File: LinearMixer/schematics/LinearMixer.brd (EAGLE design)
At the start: 49.7 x 98.7 mm, 65 parts, among them IC1 QUAD_OPAMPD, IC2 QUAD_OPAMPD, X1 53048-05, X2 53048-05, X5 53048-03, X6 53048-03, X7 53048-03

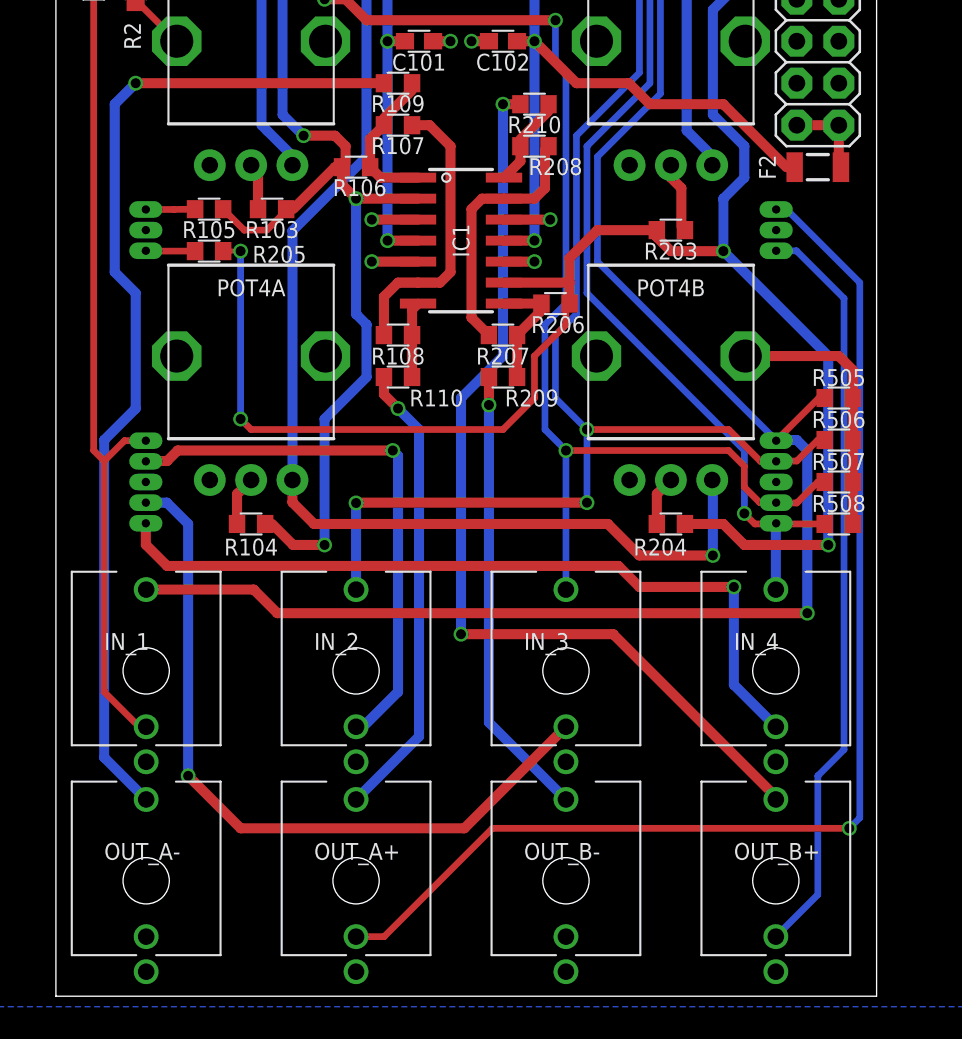
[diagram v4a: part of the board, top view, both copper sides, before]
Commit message: adjusted routing and labels, moved connector away from power inlet
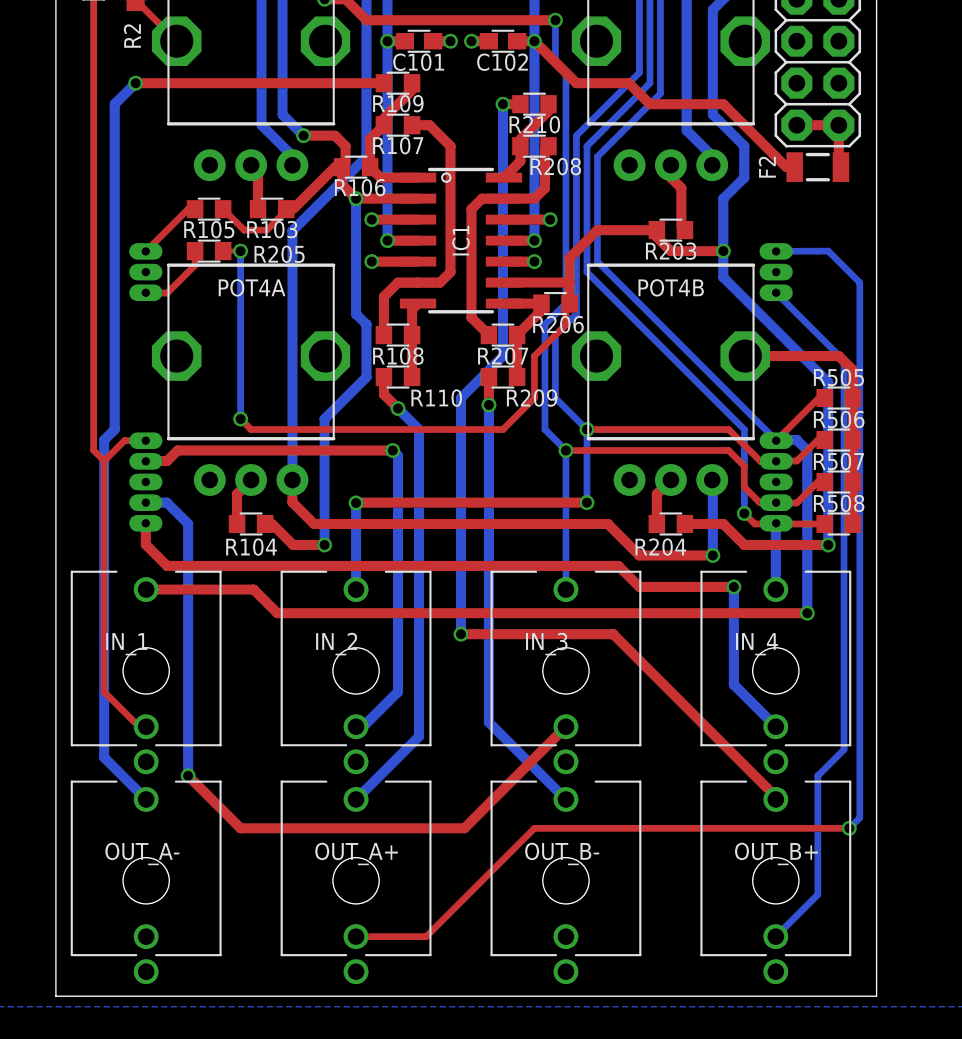
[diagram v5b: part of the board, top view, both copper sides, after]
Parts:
- moved X6 2.54 mm to (6.35, 44.5)
- moved X7 2.54 mm to (47.0, 44.5)
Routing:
- net OUT_SW_B: track 45.6 -> 42.4 mm
- net IN_B: track 2.99 -> 4.54 mm
- net OUT_SW_A: track 72.8 -> 71.7 mm
- net IN_A: track 2.98 -> 4.04 mm
- net N$11: track 61.3 -> 60.2 mm
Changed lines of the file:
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@@
 <layer number="27" name="tValues" color="7" fill="1" visible="no" active="yes"/>
 <layer number="28" name="bValues" color="7" fill="1" visible="no" active="yes"/>
-<layer number="29" name="tStop" color="7" fill="3" visible="yes" active="yes"/>
-<layer number="30" name="bStop" color="7" fill="6" visible="yes" active="yes"/>
+<layer number="29" name="tStop" color="7" fill="3" visible="no" active="yes"/>
+<layer number="30" name="bStop" color="7" fill="6" visible="no" active="yes"/>
 <layer number="31" name="tCream" color="7" fill="4" visible="no" active="yes"/>
 <layer number="32" name="bCream" color="7" fill="5" visible="no" active="yes"/>
@@
 <wire x1="2.159" y1="0.635" x2="51.816" y2="0.635" width="0" layer="20"/>
 <dimension x1="1.27" y1="0" x2="1.27" y2="100" x3="-1.27" y3="50" textsize="1.778" layer="47"/>
-<dimension x1="2.032" y1="0" x2="51.816" y2="0" x3="26.924" y3="-4.445" textsize="1.778" layer="47"/>
+<dimension x1="1.816" y1="0" x2="51.816" y2="0" x3="26.816" y3="-4.445" textsize="1.778" layer="47"/>
 <text x="4.445" y="70.485" size="1.778" layer="47" font="vector" rot="R90">Rebel Technology</text>
 <text x="6.985" y="70.485" size="1.778" layer="47" font="vector" rot="R90">LinearMixer Rev02</text>
@@
 <attribute name="NAME" x="49.53" y="37.563425" size="1.016" layer="25" font="vector" align="bottom-center"/>
 </element>
-<element name="X6" library="con-molex" package="53048-03" value="53048-03" x="6.35" y="46.99" rot="MR270">
-<attribute name="OC_NEWARK" value="38C9908" x="6.35" y="46.99" size="1.016" layer="28" rot="MR270" display="off"/>
-<attribute name="MPN" value="53048-0310" x="6.35" y="46.99" size="1.016" layer="28" rot="MR270" display="off"/>
-<attribute name="MF" value="WALDOM/MOLEX" x="6.35" y="46.99" size="1.016" layer="28" rot="MR270" display="off"/>
-<attribute name="OC_FARNELL" value="9732918" x="6.35" y="46.99" size="1.016" layer="28" rot="MR270" display="off"/>
-</element>
-<element name="X7" library="con-molex" package="53048-03" value="53048-03" x="46.99" y="46.99" rot="MR90">
-<attribute name="OC_NEWARK" value="38C9908" x="46.99" y="46.99" size="1.016" layer="28" rot="MR90" display="off"/>
-<attribute name="MPN" value="53048-0310" x="46.99" y="46.99" size="1.016" layer="28" rot="MR90" display="off"/>
-<attribute name="MF" value="WALDOM/MOLEX" x="46.99" y="46.99" size="1.016" layer="28" rot="MR90" display="off"/>
-<attribute name="OC_FARNELL" value="9732918" x="46.99" y="46.99" size="1.016" layer="28" rot="MR90" display="off"/>
+<element name="X6" library="con-molex" package="53048-03" value="53048-03" x="6.35" y="44.45" rot="MR270">
+<attribute name="OC_NEWARK" value="38C9908" x="6.35" y="44.45" size="1.016" layer="28" rot="MR270" display="off"/>
+<attribute name="MPN" value="53048-0310" x="6.35" y="44.45" size="1.016" layer="28" rot="MR270" display="off"/>
+<attribute name="MF" value="WALDOM/MOLEX" x="6.35" y="44.45" size="1.016" layer="28" rot="MR270" display="off"/>
+<attribute name="OC_FARNELL" value="9732918" x="6.35" y="44.45" size="1.016" layer="28" rot="MR270" display="off"/>
+</element>
+<element name="X7" library="con-molex" package="53048-03" value="53048-03" x="46.99" y="44.45" rot="MR90">
+<attribute name="OC_NEWARK" value="38C9908" x="46.99" y="44.45" size="1.016" layer="28" rot="MR90" display="off"/>
+<attribute name="MPN" value="53048-0310" x="46.99" y="44.45" size="1.016" layer="28" rot="MR90" display="off"/>
+<attribute name="MF" value="WALDOM/MOLEX" x="46.99" y="44.45" size="1.016" layer="28" rot="MR90" display="off"/>
+<attribute name="OC_FARNELL" value="9732918" x="46.99" y="44.45" size="1.016" layer="28" rot="MR90" display="off"/>
 </element>
 </elements>
@@
 <via x="6.985" y="55.88" extent="1-16" drill="0.6"/>
 <wire x1="6.985" y1="55.88" x2="5.715" y2="54.61" width="0.6096" layer="16"/>
-<wire x1="5.715" y1="54.61" x2="5.715" y2="44.45" width="0.6096" layer="16"/>
-<wire x1="5.715" y1="44.45" x2="6.985" y2="43.18" width="0.6096" layer="16"/>
-<wire x1="6.985" y1="43.18" x2="6.985" y2="36.195" width="0.6096" layer="16"/>
-<wire x1="6.985" y1="36.195" x2="5.08" y2="34.29" width="0.6096" layer="16"/>
+<wire x1="5.715" y1="54.61" x2="5.715" y2="34.925" width="0.6096" layer="16"/>
+<wire x1="5.715" y1="34.925" x2="5.08" y2="34.29" width="0.6096" layer="16"/>
 <wire x1="5.08" y1="34.29" x2="5.08" y2="15.08" width="0.6096" layer="16"/>
 <wire x1="5.08" y1="15.08" x2="7.62" y2="12.54" width="0.6096" layer="16"/>
@@
 <wire x1="38.1" y1="64.77" x2="38.1" y2="55.88" width="0.4064" layer="16"/>
 <wire x1="38.1" y1="55.88" x2="34.29" y2="52.07" width="0.4064" layer="16"/>
-<wire x1="34.29" y1="52.07" x2="34.29" y2="43.18" width="0.4064" layer="16"/>
-<wire x1="34.29" y1="43.18" x2="43.815" y2="33.655" width="0.4064" layer="16"/>
+<wire x1="34.29" y1="52.07" x2="34.29" y2="44.45" width="0.4064" layer="16"/>
+<wire x1="34.29" y1="44.45" x2="43.815" y2="34.925" width="0.4064" layer="16"/>
 <contactref element="R508" pad="1"/>
-<wire x1="43.815" y1="33.655" x2="43.815" y2="29.845" width="0.4064" layer="16"/>
+<wire x1="43.815" y1="34.925" x2="43.815" y2="29.845" width="0.4064" layer="16"/>
 <wire x1="43.815" y1="29.845" x2="44.45" y2="29.21" width="0.4064" layer="1"/>
 <wire x1="44.45" y1="29.21" x2="45.7" y2="29.21" width="0.4064" layer="1"/>
@@
 <wire x1="43.815" y1="27.94" x2="48.895" y2="27.94" width="0.6096" layer="1"/>
 <via x="48.895" y="27.94" extent="1-16" drill="0.6"/>
-<wire x1="48.895" y1="27.94" x2="48.895" y2="39.37" width="0.6096" layer="16"/>
-<wire x1="48.895" y1="39.37" x2="42.545" y2="45.72" width="0.6096" layer="16"/>
+<wire x1="48.895" y1="27.94" x2="48.895" y2="37.7825" width="0.6096" layer="16"/>
+<wire x1="48.895" y1="37.7825" x2="42.545" y2="44.1325" width="0.6096" layer="16"/>
+<wire x1="42.545" y1="44.1325" x2="42.545" y2="45.72" width="0.6096" layer="16"/>
 <wire x1="12.28" y1="45.72" x2="13.335" y2="45.72" width="0.3048" layer="1"/>
 <via x="13.335" y="45.72" extent="1-16" drill="0.6"/>
@@
 <signal name="IN_A">
 <contactref element="R105" pad="2"/>
-<wire x1="9.29" y1="48.24" x2="10.58" y2="48.26" width="0.4064" layer="1"/>
 <contactref element="X6" pad="3"/>
-<wire x1="9.29" y1="48.24" x2="7.6" y2="48.24" width="0.4064" layer="1"/>
+<wire x1="10.58" y1="48.26" x2="10.16" y2="48.26" width="0.4064" layer="1"/>
+<wire x1="10.16" y1="48.26" x2="7.6" y2="45.7" width="0.4064" layer="1"/>
 </signal>
 <signal name="IN_B">
 <contactref element="R205" pad="2"/>
-<wire x1="10.58" y1="45.72" x2="7.62" y2="45.72" width="0.4064" layer="1"/>
 <contactref element="X6" pad="1"/>
-<wire x1="7.62" y1="45.72" x2="7.6" y2="45.74" width="0.4064" layer="1"/>
+<wire x1="10.58" y1="45.72" x2="10.58" y2="44.87" width="0.4064" layer="1"/>
+<wire x1="10.58" y1="44.87" x2="8.89" y2="43.18" width="0.4064" layer="1"/>
+<wire x1="8.89" y1="43.18" x2="7.62" y2="43.18" width="0.4064" layer="1"/>
+<wire x1="7.62" y1="43.18" x2="7.6" y2="43.2" width="0.4064" layer="1"/>
 </signal>
 <signal name="OUT_SW_A">
@@
 <wire x1="50.8" y1="43.815" x2="50.8" y2="11.43" width="0.4064" layer="16"/>
 <wire x1="50.8" y1="11.43" x2="50.165" y2="10.795" width="0.4064" layer="16"/>
-<wire x1="46.355" y1="48.26" x2="50.8" y2="43.815" width="0.4064" layer="16"/>
-<wire x1="20.32" y1="4.24" x2="22.02" y2="4.24" width="0.4064" layer="1"/>
-<wire x1="22.02" y1="4.24" x2="28.575" y2="10.795" width="0.4064" layer="1"/>
-<wire x1="28.575" y1="10.795" x2="50.165" y2="10.795" width="0.4064" layer="1"/>
+<wire x1="48.895" y1="45.72" x2="50.8" y2="43.815" width="0.4064" layer="16"/>
+<wire x1="20.32" y1="4.24" x2="24.56" y2="4.24" width="0.4064" layer="1"/>
+<wire x1="24.56" y1="4.24" x2="31.115" y2="10.795" width="0.4064" layer="1"/>
+<wire x1="31.115" y1="10.795" x2="50.165" y2="10.795" width="0.4064" layer="1"/>
 <via x="50.165" y="10.795" extent="1-16" drill="0.6"/>
 <contactref element="X7" pad="1"/>
-<wire x1="45.74" y1="48.24" x2="45.72" y2="48.26" width="0.4064" layer="16"/>
-<wire x1="45.72" y1="48.26" x2="46.355" y2="48.26" width="0.4064" layer="16"/>
+<wire x1="45.74" y1="45.7" x2="48.26" y2="45.72" width="0.4064" layer="16"/>
+<wire x1="48.26" y1="45.72" x2="48.895" y2="45.72" width="0.4064" layer="16"/>
 </signal>
 <signal name="OUT_SW_B">
 <contactref element="OUT_B+" pad="P$2"/>
-<wire x1="49.8475" y1="15.5575" x2="49.8475" y2="42.8625" width="0.4064" layer="16"/>
+<wire x1="49.8475" y1="15.5575" x2="49.8475" y2="39.0925" width="0.4064" layer="16"/>
 <wire x1="49.8475" y1="15.5575" x2="48.26" y2="13.97" width="0.4064" layer="16"/>
 <wire x1="48.26" y1="13.97" x2="48.26" y2="6.78" width="0.4064" layer="16"/>
 <wire x1="48.26" y1="6.78" x2="45.72" y2="4.24" width="0.4064" layer="16"/>
 <contactref element="X7" pad="3"/>
-<wire x1="45.74" y1="45.74" x2="46.97" y2="45.74" width="0.4064" layer="16"/>
-<wire x1="46.97" y1="45.74" x2="49.8475" y2="42.8625" width="0.4064" layer="16"/>
+<wire x1="49.8475" y1="39.0925" x2="45.74" y2="43.2" width="0.4064" layer="16"/>
 </signal>
 <signal name="N$7">

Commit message: rev02 ordered from seeed
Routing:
- net IN_2: track 75.2 -> 72.7 mm, vias 4 -> 3
- net IN_4: vias 2 -> 1
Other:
- board text added: "-12V"
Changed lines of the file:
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@@
 <dimension x1="1.27" y1="0" x2="1.27" y2="100" x3="-1.27" y3="50" textsize="1.778" layer="47"/>
 <dimension x1="1.816" y1="0" x2="51.816" y2="0" x3="26.816" y3="-4.445" textsize="1.778" layer="47"/>
-<text x="4.445" y="70.485" size="1.778" layer="47" font="vector" rot="R90">Rebel Technology</text>
-<text x="6.985" y="70.485" size="1.778" layer="47" font="vector" rot="R90">LinearMixer Rev02</text>
-<text x="13.97" y="85.725" size="1.778" layer="47" font="vector" rot="MR180">Rebel Technology</text>
-<text x="12.7" y="82.55" size="1.778" layer="47" font="vector" rot="MR180">LinearMixer Rev02</text>
+<text x="4.445" y="70.485" size="1.778" layer="21" font="vector" rot="R90">Rebel Technology</text>
+<text x="6.985" y="70.485" size="1.778" layer="21" font="vector" rot="R90">LinearMixer Rev02</text>
+<text x="13.97" y="85.725" size="1.778" layer="22" font="vector" rot="MR180">Rebel Technology</text>
+<text x="12.7" y="82.55" size="1.778" layer="22" font="vector" rot="MR180">LinearMixer Rev02</text>
+<text x="48.26" y="49.276" size="1.27" layer="25" font="vector" align="top-center">-12V</text>
+<text x="48.26" y="49.276" size="1.27" layer="22" font="vector" rot="MR0" align="top-center">-12V</text>
 </plain>
 <attributes>
@@
 </element>
 <element name="IN_2" library="Rebel" package="THONKICONN" value="THONKICONN" x="20.32" y="20.32" smashed="yes">
-<attribute name="NAME" x="17.78" y="21.59" size="1.016" layer="25"/>
+<attribute name="NAME" x="17.78" y="22.86" size="1.016" layer="25"/>
 </element>
 <element name="IN_3" library="Rebel" package="THONKICONN" value="THONKICONN" x="33.02" y="20.32" smashed="yes">
-<attribute name="NAME" x="30.48" y="21.59" size="1.016" layer="25"/>
+<attribute name="NAME" x="30.48" y="22.86" size="1.016" layer="25"/>
 </element>
 <element name="IN_4" library="Rebel" package="THONKICONN" value="THONKICONN" x="45.72" y="20.32" smashed="yes">
-<attribute name="NAME" x="43.18" y="21.59" size="1.016" layer="25"/>
+<attribute name="NAME" x="43.18" y="22.86" size="1.016" layer="25"/>
 </element>
 <element name="IN_1" library="Rebel" package="THONKICONN" value="THONKICONN" x="7.62" y="20.32" smashed="yes">
-<attribute name="NAME" x="5.08" y="21.59" size="1.016" layer="25"/>
+<attribute name="NAME" x="5.08" y="22.86" size="1.016" layer="25"/>
 </element>
 <element name="IC2" library="adafruit" package="SO14" value="QUAD_OPAMPD" x="26.67" y="67.31" smashed="yes" rot="R270">
@@
 </element>
 <element name="OUT_A+" library="Rebel" package="THONKICONN" value="THONKICONN" x="20.32" y="7.62" smashed="yes">
-<attribute name="NAME" x="17.78" y="8.89" size="1.016" layer="25"/>
+<attribute name="NAME" x="17.78" y="10.16" size="1.016" layer="25"/>
 </element>
 <element name="OUT_A-" library="Rebel" package="THONKICONN" value="THONKICONN" x="7.62" y="7.62" smashed="yes">
-<attribute name="NAME" x="5.08" y="8.89" size="1.016" layer="25"/>
+<attribute name="NAME" x="5.08" y="10.16" size="1.016" layer="25"/>
 </element>
 <element name="OUT_B+" library="Rebel" package="THONKICONN" value="THONKICONN" x="45.72" y="7.62" smashed="yes">
-<attribute name="NAME" x="43.18" y="8.89" size="1.016" layer="25"/>
+<attribute name="NAME" x="43.18" y="10.16" size="1.016" layer="25"/>
 </element>
 <element name="OUT_B-" library="Rebel" package="THONKICONN" value="THONKICONN" x="33.02" y="7.62" smashed="yes">
-<attribute name="NAME" x="30.48" y="8.89" size="1.016" layer="25"/>
+<attribute name="NAME" x="30.48" y="10.16" size="1.016" layer="25"/>
 </element>
 <element name="R104" library="resistor" package="R0603" value="100k" x="13.97" y="29.21" smashed="yes" rot="R180">
@@
 <contactref element="R505" pad="1"/>
 <wire x1="45.74" y1="34.25" x2="45.74" y2="34.27" width="0.4064" layer="16"/>
-<wire x1="47.625" y1="23.8125" x2="47.625" y2="33.655" width="0.6096" layer="16"/>
-<wire x1="47.625" y1="33.655" x2="46.99" y2="34.29" width="0.6096" layer="16"/>
-<wire x1="46.99" y1="34.29" x2="45.78" y2="34.29" width="0.6096" layer="16"/>
+<wire x1="47.625" y1="23.8125" x2="47.625" y2="33.655" width="0.4064" layer="16"/>
+<wire x1="47.625" y1="33.655" x2="46.99" y2="34.29" width="0.4064" layer="16"/>
+<wire x1="46.99" y1="34.29" x2="45.78" y2="34.29" width="0.4064" layer="16"/>
 <wire x1="45.78" y1="34.29" x2="45.74" y2="34.25" width="0.6096" layer="16"/>
 <wire x1="48.68" y1="36.83" x2="48.32" y2="36.83" width="0.4064" layer="1"/>
@@
 <contactref element="R508" pad="1"/>
 <wire x1="43.815" y1="34.925" x2="43.815" y2="29.845" width="0.4064" layer="16"/>
-<wire x1="43.815" y1="29.845" x2="44.45" y2="29.21" width="0.4064" layer="1"/>
-<wire x1="44.45" y1="29.21" x2="45.7" y2="29.21" width="0.4064" layer="1"/>
+<wire x1="43.815" y1="29.845" x2="44.45" y2="29.21" width="0.4064" layer="16"/>
+<wire x1="44.45" y1="29.21" x2="45.7" y2="29.21" width="0.4064" layer="16"/>
+<wire x1="45.7" y1="29.21" x2="45.74" y2="29.25" width="0.4064" layer="16"/>
+<wire x1="48.68" y1="29.21" x2="45.78" y2="29.21" width="0.4064" layer="1"/>
+<wire x1="45.78" y1="29.21" x2="45.74" y2="29.25" width="0.4064" layer="1"/>
 <wire x1="45.72" y1="25.24" x2="45.72" y2="29.23" width="0.6096" layer="16"/>
 <wire x1="45.72" y1="29.23" x2="45.74" y2="29.25" width="0.6096" layer="16"/>
-<wire x1="48.68" y1="29.21" x2="45.78" y2="29.21" width="0.4064" layer="1"/>
-<via x="43.815" y="29.845" extent="1-16" drill="0.6"/>
-<wire x1="45.7" y1="29.21" x2="45.74" y2="29.25" width="0.6096" layer="1"/>
-<wire x1="45.74" y1="29.25" x2="45.78" y2="29.21" width="0.6096" layer="1"/>
 </signal>
 <signal name="IN_3">
@@
 <contactref element="R503" pad="2"/>
 <contactref element="X2" pad="4"/>
-<wire x1="33.02" y1="33.655" x2="33.02" y2="25.24" width="0.4064" layer="16"/>
+<wire x1="33.02" y1="33.655" x2="33.02" y2="25.24" width="0.6096" layer="16"/>
 <wire x1="19.47" y1="65.405" x2="18.415" y2="65.405" width="0.6096" layer="1"/>
 <via x="18.415" y="65.405" extent="1-16" drill="0.6"/>
@@
 <contactref element="R502" pad="2"/>
 <contactref element="X2" pad="2"/>
-<wire x1="34.29" y1="30.5" x2="20.34" y2="30.5" width="0.6096" layer="1"/>
 <wire x1="20.34" y1="30.5" x2="20.32" y2="30.48" width="0.3048" layer="1"/>
 <via x="20.32" y="30.48" extent="1-16" drill="0.6"/>
@@
 <wire x1="32.385" y1="40.64" x2="32.385" y2="36.83" width="0.4064" layer="16"/>
 <wire x1="32.385" y1="36.83" x2="34.29" y2="34.925" width="0.4064" layer="16"/>
-<via x="34.29" y="30.5" extent="1-16" drill="0.6"/>
 <contactref element="R506" pad="1"/>
-<wire x1="34.29" y1="34.925" x2="34.29" y2="30.5" width="0.4064" layer="16"/>
 <wire x1="45.74" y1="33" x2="44.7875" y2="33" width="0.4064" layer="1"/>
 <wire x1="44.7875" y1="33" x2="42.8625" y2="34.925" width="0.4064" layer="1"/>
@@
 <wire x1="46.99" y1="33.02" x2="45.76" y2="33.02" width="0.4064" layer="1"/>
 <wire x1="45.76" y1="33.02" x2="45.74" y2="33" width="0.4064" layer="1"/>
+<wire x1="34.29" y1="34.925" x2="32.385" y2="34.925" width="0.6096" layer="1"/>
+<wire x1="32.385" y1="34.925" x2="27.94" y2="30.48" width="0.6096" layer="1"/>
+<wire x1="27.94" y1="30.48" x2="20.32" y2="30.48" width="0.6096" layer="1"/>
 </signal>
 <signal name="IN_SW_4">
@@
 <signal name="OUT_SW_B">
 <contactref element="OUT_B+" pad="P$2"/>
-<wire x1="49.8475" y1="15.5575" x2="49.8475" y2="39.0925" width="0.4064" layer="16"/>
-<wire x1="49.8475" y1="15.5575" x2="48.26" y2="13.97" width="0.4064" layer="16"/>
-<wire x1="48.26" y1="13.97" x2="48.26" y2="6.78" width="0.4064" layer="16"/>
+<wire x1="49.8475" y1="23.1775" x2="49.8475" y2="39.0925" width="0.4064" layer="16"/>
+<wire x1="49.8475" y1="23.1775" x2="48.26" y2="21.59" width="0.4064" layer="16"/>
+<wire x1="48.26" y1="21.59" x2="48.26" y2="6.78" width="0.4064" layer="16"/>
 <wire x1="48.26" y1="6.78" x2="45.72" y2="4.24" width="0.4064" layer="16"/>
 <contactref element="X7" pad="3"/>

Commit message: changed daisy input resistor values to ensure unity gain
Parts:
- R105, R205: value 100k -> 200k
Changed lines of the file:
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@@
 <attribute name="NAME" x="39.37" y="93.155" size="1.016" layer="25" font="vector" align="bottom-center"/>
 </element>
-<element name="R105" library="resistor" package="R0603" value="100k" x="11.43" y="48.26" smashed="yes" rot="R180">
+<element name="R105" library="resistor" package="R0603" value="200k" x="11.43" y="48.26" smashed="yes" rot="R180">
 <attribute name="NAME" x="11.43" y="47.52975" size="1.016" layer="25" font="vector" rot="R180" align="bottom-center"/>
 </element>
-<element name="R205" library="resistor" package="R0603" value="100k" x="11.43" y="45.72" smashed="yes" rot="R180">
+<element name="R205" library="resistor" package="R0603" value="200k" x="11.43" y="45.72" smashed="yes" rot="R180">
 <attribute name="NAME" x="15.6845" y="46.0375" size="1.016" layer="25" font="vector" rot="R180" align="bottom-center"/>
 </element>
